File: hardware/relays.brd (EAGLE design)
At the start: 114.5 x 51.6 mm, 19 parts, among them U1 MMBT2222ALT1G, U2 MMBT2222ALT1G

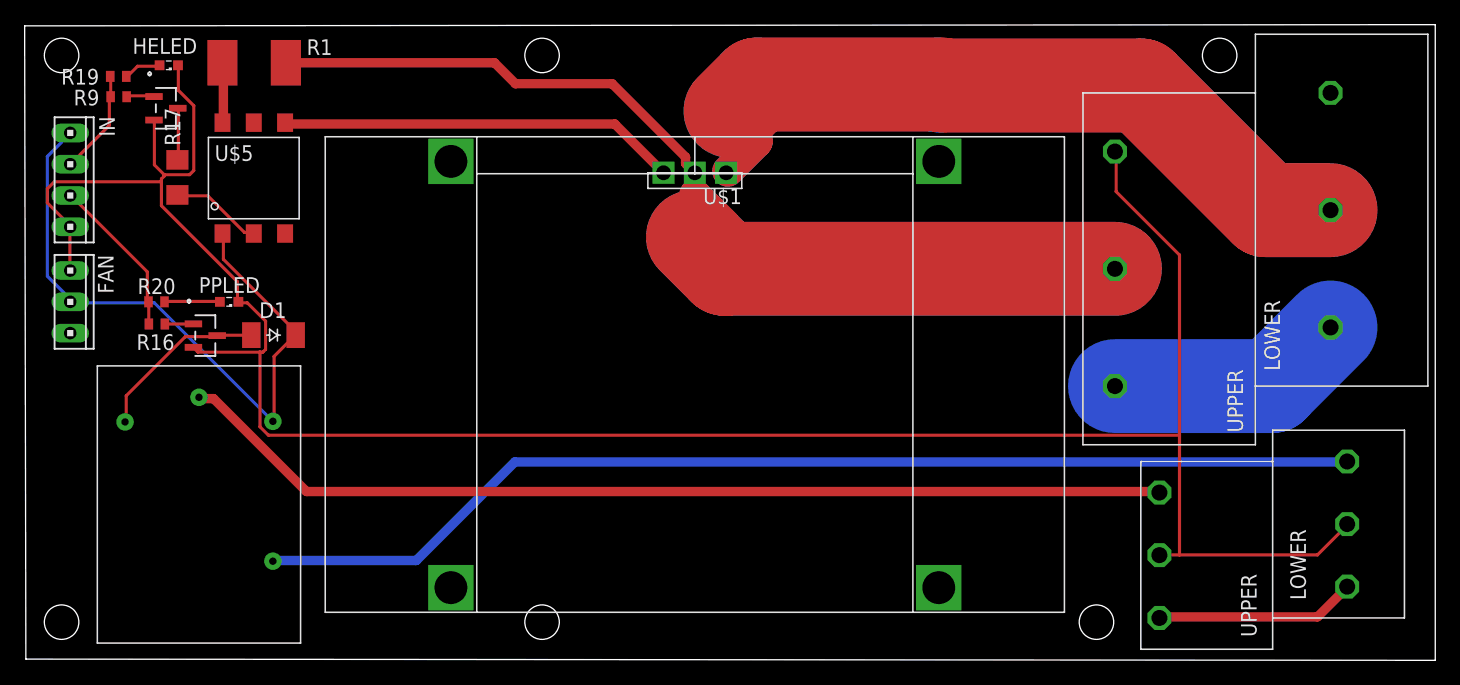
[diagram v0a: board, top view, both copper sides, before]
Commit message: IO and Relay boards are distinct
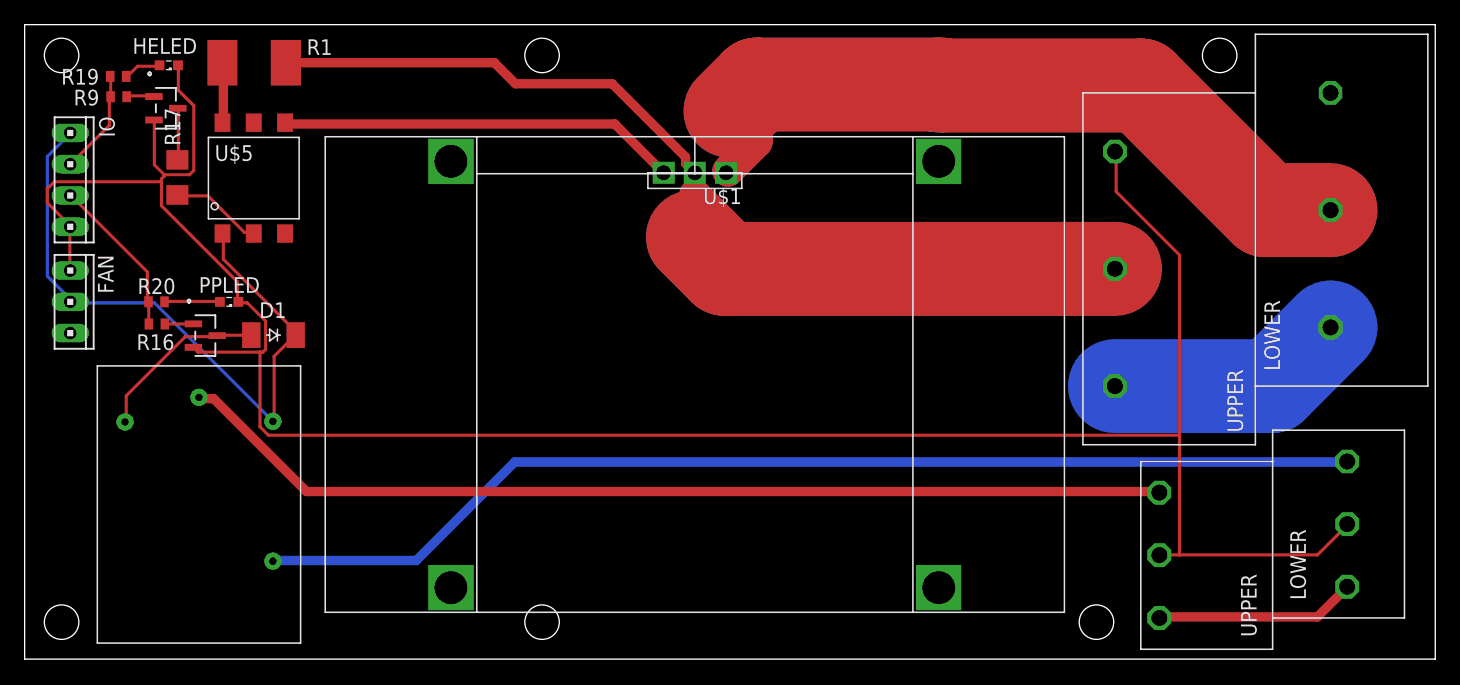
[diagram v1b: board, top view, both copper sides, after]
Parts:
- renumbered IN to IO
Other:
- board size 114.5 x 51.6 mm -> 114.5 x 51.5 mm
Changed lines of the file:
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@@
 <board>
 <plain>
-<wire x1="0.1" y1="0" x2="114.5" y2="-0.1" width="0" layer="20"/>
-<wire x1="114.5" y1="-0.1" x2="114.5" y2="51.5" width="0" layer="20"/>
-<wire x1="114.5" y1="51.5" x2="0" y2="51.4" width="0" layer="20"/>
-<wire x1="0" y1="51.4" x2="0.1" y2="0" width="0" layer="20"/>
+<wire x1="0" y1="0" x2="114.5" y2="0" width="0" layer="20"/>
+<wire x1="114.5" y1="0" x2="114.5" y2="51.5" width="0" layer="20"/>
+<wire x1="114.5" y1="51.5" x2="0" y2="51.5" width="0" layer="20"/>
+<wire x1="0" y1="51.5" x2="0" y2="0" width="0" layer="20"/>
 <hole x="3" y="49" drill="2.8"/>
 <hole x="42" y="49" drill="2.8"/>
@@
 <element name="U$4" library="digikey" package="PC-MKKDS1.5/3-5.08" value="PC1725041" x="112" y="0.8" rot="R90"/>
 <element name="U$6" library="digikey" package="PC-MKKDS5/3-9.5" value="PC1719028" x="113.9" y="17.4" rot="R90"/>
-<element name="IN" library="con-amp" library_urn="urn:adsk.eagle:library:127" package="10X04MTA" value="" x="3.7" y="38.9" smashed="yes" rot="R270">
+<element name="IO" library="con-amp" library_urn="urn:adsk.eagle:library:127" package="10X04MTA" value="" x="3.7" y="38.9" smashed="yes" rot="R270">
 <attribute name="NAME" x="6.0488" y="44.0512" size="1.27" layer="25" rot="R270"/>
 <attribute name="VALUE" x="5.8509" y="43.8761" size="1.27" layer="27" rot="R270"/>
@@
 <contactref element="U$4" pad="P$5"/>
 <contactref element="U$4" pad="P$2"/>
-<contactref element="IN" pad="1"/>
+<contactref element="IO" pad="1"/>
 <contactref element="FAN" pad="3"/>
 <contactref element="U$6" pad="P$6"/>
@@
 <contactref element="U$3" pad="P$4"/>
 <contactref element="D1" pad="C"/>
-<contactref element="IN" pad="4"/>
+<contactref element="IO" pad="4"/>
 <contactref element="FAN" pad="2"/>
 <wire x1="3.6723" y1="29.2608" x2="3.6723" y2="29.0322" width="0.254" layer="16"/>
@@
 <contactref element="R9" pad="2"/>
 <contactref element="R19" pad="1"/>
-<contactref element="IN" pad="3"/>
+<contactref element="IO" pad="3"/>
 <wire x1="6.987" y1="45.72" x2="6.987" y2="47.2059" width="0.254" layer="1"/>
 <wire x1="6.987" y1="47.2059" x2="6.95" y2="47.3" width="0.254" layer="1"/>
@@
 <contactref element="R16" pad="2"/>
 <contactref element="R20" pad="1"/>
-<contactref element="IN" pad="2"/>
+<contactref element="IO" pad="2"/>
 <wire x1="10.0731" y1="27.2034" x2="10.0731" y2="28.9179" width="0.254" layer="1"/>
 <wire x1="10.0731" y1="28.9179" x2="10.05" y2="29" width="0.254" layer="1"/>

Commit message: Fix relay holes, triac holes and orientation, and DRC issues.
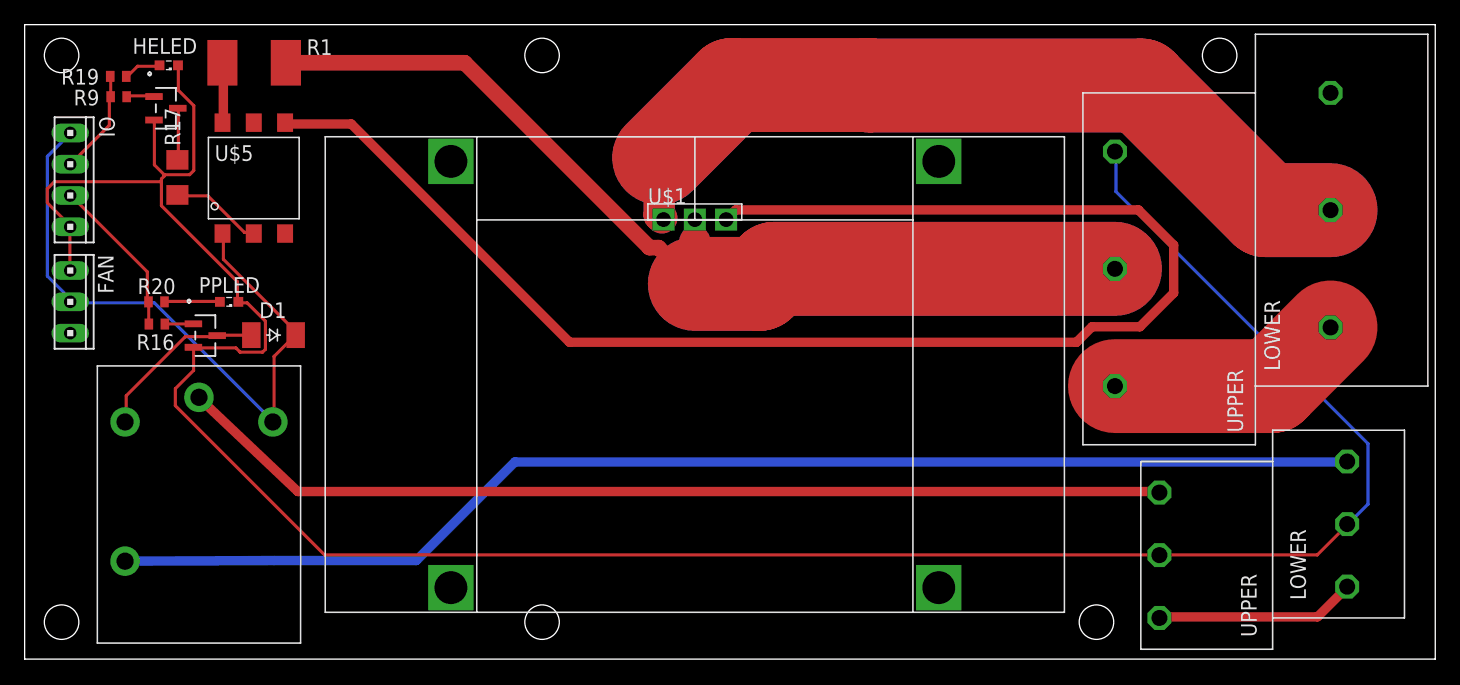
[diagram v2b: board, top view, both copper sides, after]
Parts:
- moved U$1 3.80 mm to (54.4, 35.7), turned to 0 degrees
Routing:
- net N$19: track 32.5 -> 123.0 mm
- net GND: track 189.8 -> 203.7 mm
- net 120H: track 90.6 -> 102.5 mm
- net -120: track 123.6 -> 132.8 mm
